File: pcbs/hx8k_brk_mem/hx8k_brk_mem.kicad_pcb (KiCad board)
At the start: 2 copper layers, 127 x 76.2 mm, 23 parts, among them J1 CONN_02X20, J2 CONN_02X20, U1 AS6C4008, U2 AS6C4008, U3 AS6C4008, U4 AS6C4008, U5 AS6C62256, U6 AS6C62256, U7 74HC04, U8 74HC32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

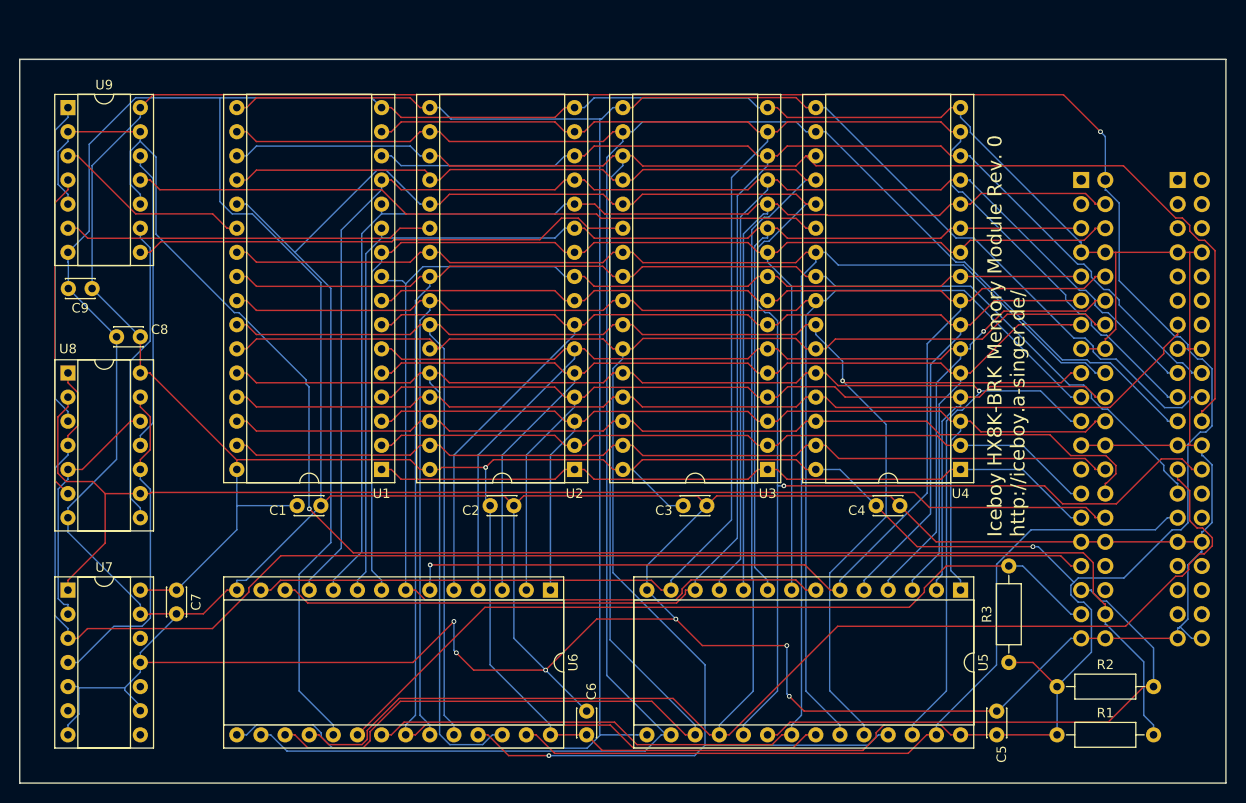
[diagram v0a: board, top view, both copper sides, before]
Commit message: Migrate memory pcb from KiCad 4 to KiCad 8
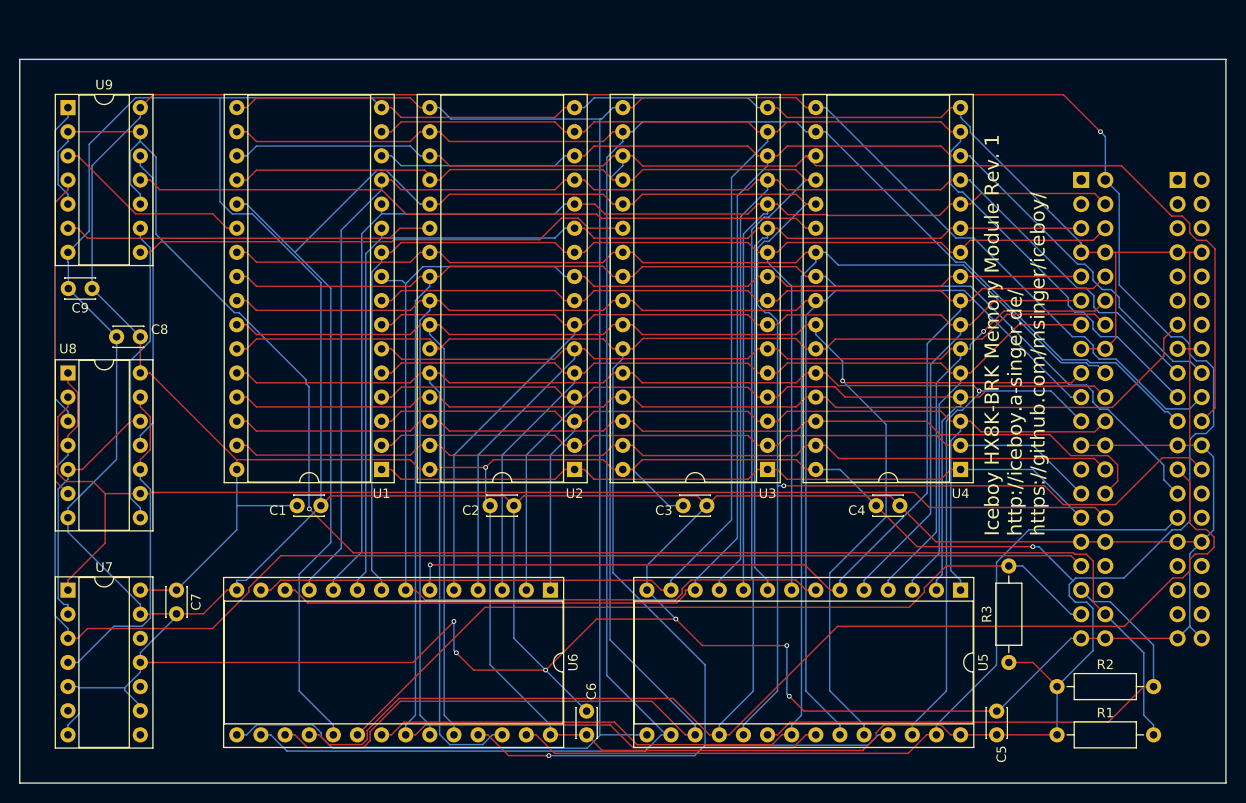
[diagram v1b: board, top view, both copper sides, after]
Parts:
- C1, C2, C3, C4, C5, C6, C7, C8, C9: footprint Capacitors_THT:C_Disc_D3.0mm_W2.0mm_P2.50mm -> Capacitor_THT:C_Disc_D3.0mm_W2.0mm_P2.50mm
- J1, J2: value CONN_02X20 -> Conn_02x20_Odd_Even; footprint Pin_Headers:Pin_Header_Straight_2x20_Pitch2.54mm -> Connector_PinSocket_2.54mm:PinSocket_2x20_P2.54mm_Vertical
- R1, R2, R3: footprint Resistors_THT:R_Axial_DIN0207_L6.3mm_D2.5mm_P10.16mm_Horizontal -> Resistor_THT:R_Axial_DIN0207_L6.3mm_D2.5mm_P10.16mm_Horizontal
- U1, U2, U3, U4: footprint Housings_DIP:DIP-32_W15.24mm_Socket -> Package_DIP:DIP-32_W15.24mm_Socket
- U5, U6: footprint Housings_DIP:DIP-28_W15.24mm_Socket -> Package_DIP:DIP-28_W15.24mm_Socket
- U7, U8, U9: footprint Housings_DIP:DIP-14_W7.62mm_Socket -> Package_DIP:DIP-14_W7.62mm_Socket
- moved J1 2.55 mm to (198.1, 63.5)
- moved J2 2.54 mm to (188.0, 63.5)
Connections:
- net /Demux/~CS0 renamed /Demux/~{CS0}
- net /Demux/~CS1 renamed /Demux/~{CS1}
- net /Demux/~CS2 renamed /Demux/~{CS2}
- net /Demux/~CS3 renamed /Demux/~{CS3}
- net /~CSROM renamed /~{CSROM}
- net /~CSWRAM renamed /~{CSWRAM}
- net /~CSXRAM renamed /~{CSXRAM}
- net /~PROG renamed /~{PROG}
- net /~RD renamed /~{RD}
- net /~WR renamed /~{WR}
- J1 pad 1: Net-(J1-Pad1) -> unconnected-(J1-Pin_1-Pad1)
- J1 pad 10: Net-(J1-Pad10) -> unconnected-(J1-Pin_10-Pad10)
- J1 pad 11: Net-(J1-Pad11) -> unconnected-(J1-Pin_11-Pad11)
- J1 pad 12: Net-(J1-Pad12) -> unconnected-(J1-Pin_12-Pad12)
- J1 pad 14: Net-(J1-Pad14) -> unconnected-(J1-Pin_14-Pad14)
- J1 pad 2: Net-(J1-Pad2) -> unconnected-(J1-Pin_2-Pad2)
- J1 pad 28: Net-(J1-Pad28) -> unconnected-(J1-Pin_28-Pad28)
- J1 pad 3: Net-(J1-Pad3) -> unconnected-(J1-Pin_3-Pad3)
- J1 pad 30: Net-(J1-Pad30) -> unconnected-(J1-Pin_30-Pad30)
- J1 pad 33: Net-(J1-Pad33) -> unconnected-(J1-Pin_33-Pad33)
- J1 pad 34: Net-(J1-Pad34) -> unconnected-(J1-Pin_34-Pad34)
- J1 pad 35: Net-(J1-Pad35) -> unconnected-(J1-Pin_35-Pad35)
- J1 pad 36: Net-(J1-Pad36) -> unconnected-(J1-Pin_36-Pad36)
- J1 pad 37: Net-(J1-Pad37) -> unconnected-(J1-Pin_37-Pad37)
- J1 pad 38: Net-(J1-Pad38) -> unconnected-(J1-Pin_38-Pad38)
- J1 pad 4: Net-(J1-Pad4) -> unconnected-(J1-Pin_4-Pad4)
- J1 pad 5: Net-(J1-Pad5) -> unconnected-(J1-Pin_5-Pad5)
- J1 pad 6: Net-(J1-Pad6) -> unconnected-(J1-Pin_6-Pad6)
- J1 pad 9: Net-(J1-Pad9) -> unconnected-(J1-Pin_9-Pad9)
- J2 pad 1: Net-(J2-Pad1) -> unconnected-(J2-Pin_1-Pad1)
- J2 pad 25: Net-(J2-Pad25) -> unconnected-(J2-Pin_25-Pad25)
- J2 pad 3: Net-(J2-Pad3) -> unconnected-(J2-Pin_3-Pad3)
- J2 pad 34: Net-(J2-Pad34) -> unconnected-(J2-Pin_34-Pad34)
- J2 pad 36: Net-(J2-Pad36) -> unconnected-(J2-Pin_36-Pad36)
- U7 pad 10: Net-(U7-Pad10) -> unconnected-(U7-Pad10)
- U7 pad 12: Net-(U7-Pad12) -> unconnected-(U7-Pad12)
- U7 pad 6: Net-(U7-Pad6) -> unconnected-(U7-Pad6)
- U7 pad 8: Net-(U7-Pad8) -> unconnected-(U7-Pad8)
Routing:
- net VCC: track 453.6 -> 455.3 mm
- net GND: track 624.3 -> 623.1 mm
- net /D6: track 246.0 -> 247.0 mm
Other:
- net class Default removed
- board text added: "${TITLE} Rev. ${REVISION} ${COMMENT2} ${COMMENT1}"
- board text removed: "Iceboy HX8K-BRK Memory Module Rev. 0 http://iceboy.a-singer.de/"
